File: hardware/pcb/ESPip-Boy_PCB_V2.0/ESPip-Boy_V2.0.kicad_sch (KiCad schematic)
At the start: 106 parts, among them CN1 1X4, Q1 SS8050/Y1, Q2 SS8050/Y1, Q3 DMG1012T-7, Q4 DMG1012T-7, Q5 SS8050/Y1, SW1 SW-SMD_L4.7-W3.5-P3.35-EH, SW2 SW-SMD_L4.7-W3.5-P3.35-EH, U1 LTR-390UV-01, U10 ICS-43434_C5656610, U11 ME6217A33PG, U12 BQ24074RGTR, U13 MAX30102EFD+T_C6454833, U14 BQ27421YZFR-G1A, U17 MAX98357AETE+T, U18 ME6206B18XG, U2 CP2102N-A02-GQFN28R, U3 0402 Blue, U4 GT-USB-7010ASV, U5 BMI270, U7 YSN8010SJ 32.768KHZ, U8 ESP32-WROOM-32E(8MB), U9 LIS2MDLTR

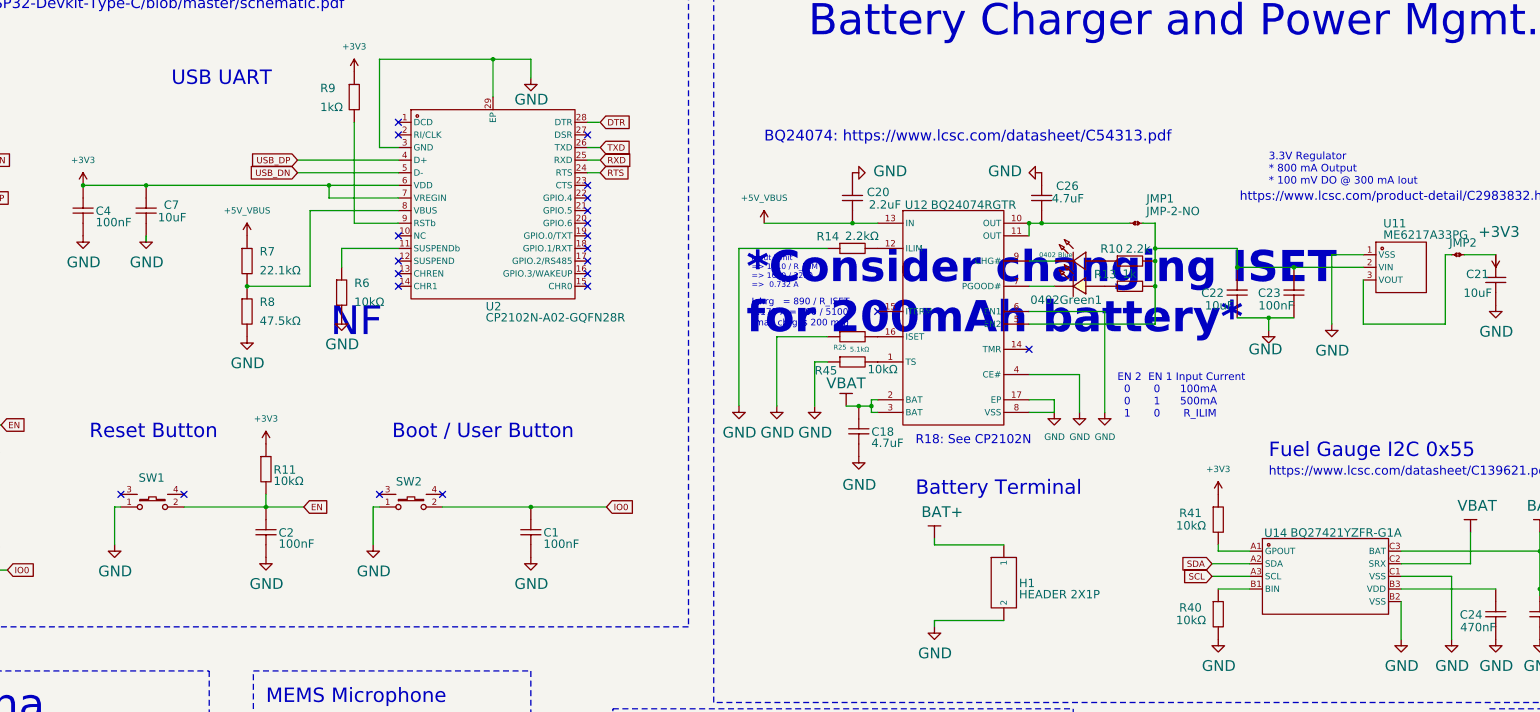
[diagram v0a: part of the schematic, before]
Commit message: V2.0 finished. All hardware verified, only motor and microphone not working as expected
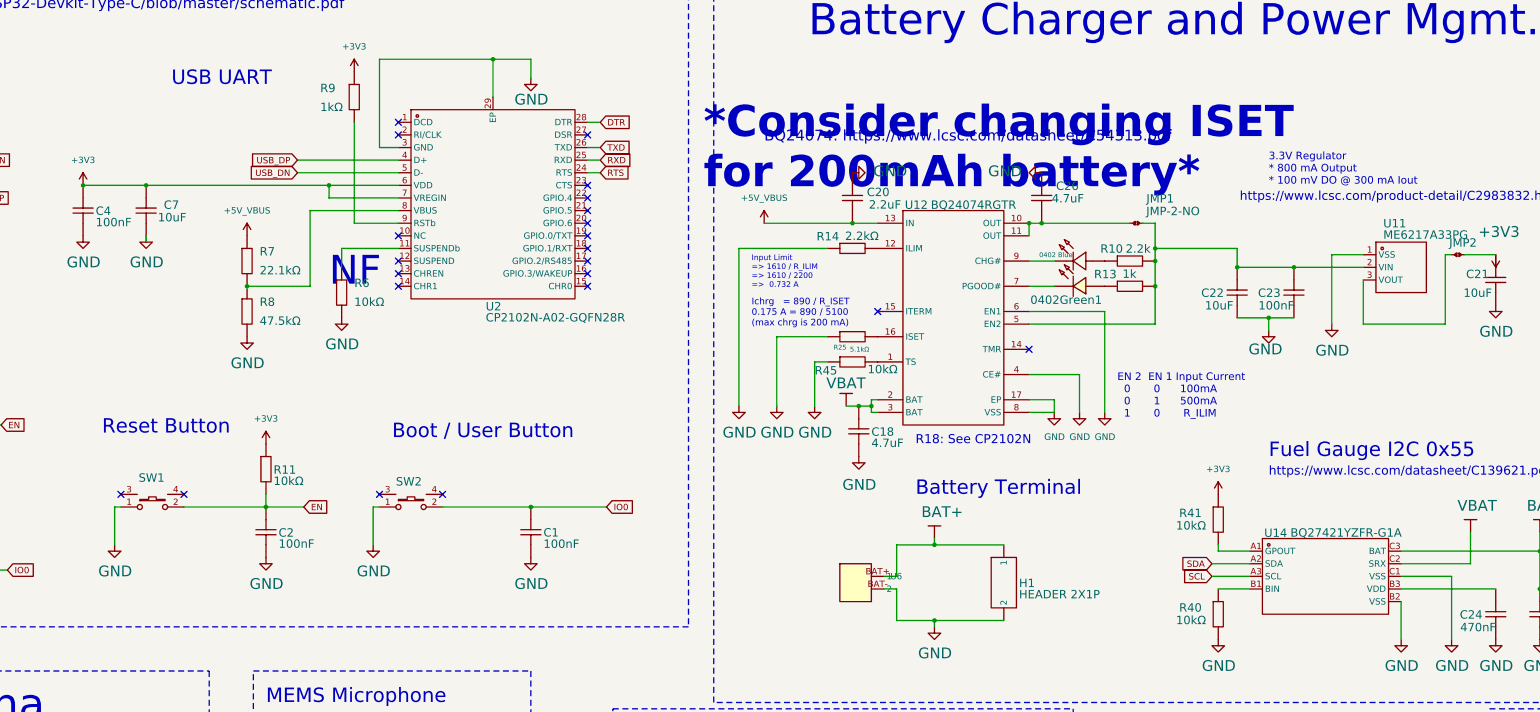
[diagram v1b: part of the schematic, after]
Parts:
- added U6: ~, 1_custom_fp_lib:200_mah_lipo, symbol 1_custom_sym_lib:200_mah_lipo
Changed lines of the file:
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@@
 	(text "NF"
 		(exclude_from_sim no)
-		(at 183.134 100.33 0)
+		(at 182.88 90.17 0)
 		(effects
 			(font
@@
 	(text "*Consider changing ISET \nfor 200mAh battery*"
 		(exclude_from_sim no)
-		(at 266.954 89.154 0)
+		(at 258.318 59.944 0)
 		(effects
 			(font
@@
 	(text "Reset Button"
 		(exclude_from_sim no)
-		(at 134.62 124.1044 0)
+		(at 137.16 123.19 0)
 		(effects
 			(font
@@
 	)
 	(junction
+		(at 304.8 163.83)
+		(diameter 0)
+		(color 0 0 0 0)
+	)
+	(junction
 		(at 284.48 354.33)
 		(diameter 0)
@@
 	)
 	(junction
+		(at 304.8 148.59)
+		(diameter 0)
+		(color 0 0 0 0)
+	)
+	(junction
 		(at 69.85 374.65)
 		(diameter 0)
@@
 	(wire
 		(pts
+			(xy 294.64 157.48) (xy 297.18 157.48)
+		)
+		(stroke
+			(width 0)
+			(type default)
+		)
+	)
+	(wire
+		(pts
 			(xy 304.8 201.93) (xy 309.88 201.93)
 		)
@@
 	(wire
 		(pts
+			(xy 294.64 154.94) (xy 297.18 154.94)
+		)
+		(stroke
+			(width 0)
+			(type default)
+		)
+	)
+	(wire
+		(pts
 			(xy 238.76 374.65) (xy 238.76 379.73)
 		)
@@
 	(wire
 		(pts
+			(xy 297.18 148.59) (xy 304.8 148.59)
+		)
+		(stroke
+			(width 0)
+			(type default)
+		)
+	)
+	(wire
+		(pts
 			(xy 320.04 275.59) (xy 320.04 281.94)
 		)
@@
 	(wire
 		(pts
+			(xy 297.18 148.59) (xy 297.18 154.94)
+		)
+		(stroke
+			(width 0)
+			(type default)
+		)
+	)
+	(wire
+		(pts
 			(xy 195.58 194.31) (xy 199.39 194.31)
 		)
@@
 	(wire
 		(pts
+			(xy 297.18 157.48) (xy 297.18 163.83)
+		)
+		(stroke
+			(width 0)
+			(type default)
+		)
+	)
+	(wire
+		(pts
 			(xy 297.18 335.28) (xy 297.18 344.17)
 		)
@@
 	(wire
 		(pts
+			(xy 297.18 163.83) (xy 304.8 163.83)
+		)
+		(stroke
+			(width 0)
+			(type default)
+		)
+	)
+	(wire
+		(pts
 			(xy 154.94 354.33) (xy 139.7 354.33)
 		)
@@
 					(unit 1)
 				)
+			)
+		)
+	)
+	(symbol
+		(lib_id "1_custom_sym_lib:200_mah_lipo")
+		(at 287.02 153.67 0)
+		(unit 1)
+		(exclude_from_sim no)
+		(in_bom yes)
+		(on_board yes)
+		(dnp no)
+		(fields_autoplaced yes)
+		(property "Reference" "U6"
+			(at 295.91 154.9399 0)
+			(effects
+				(font
+					(size 1.27 1.27)
+				)
+				(justify left)
+			)
+		)
+		(property "Value" "~"
+			(at 295.91 157.4799 0)
+			(effects
+				(font
+					(size 1.27 1.27)
+				)
+				(justify left)
+			)
+		)
+		(property "Footprint" "1_custom_fp_lib:200_mah_lipo"
+			(at 287.02 153.67 0)
+			(effects
+				(font
+					(size 1.27 1.27)
+				)
+				(hide yes)
+			)
+		)
+		(property "Datasheet" ""
+			(at 287.02 153.67 0)
+			(effects
+				(font
+					(size 1.27 1.27)
+				)
+				(hide yes)
+			)
+		)
+		(property "Description" ""
+			(at 287.02 153.67 0)
+			(effects
+				(font
+					(size 1.27 1.27)
+				)
+				(hide yes)
+			)
+		)
+		(pin "BAT+"
+		)
+		(pin "BAT-"
+		)
+		(instances
+			(project ""
+				(path "/a0672f88-4530-421b-ba73-6da91a940693"
+					(reference "U6")
+					(unit 1)
+				)
